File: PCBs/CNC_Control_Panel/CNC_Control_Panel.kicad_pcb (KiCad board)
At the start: 2 copper layers, 65 x 56 mm, 22 parts, among them J1 Conn_01x07_Male, P1 Conn_02x20_Odd_Even, X0 SW_Push, Y0 SW_Push

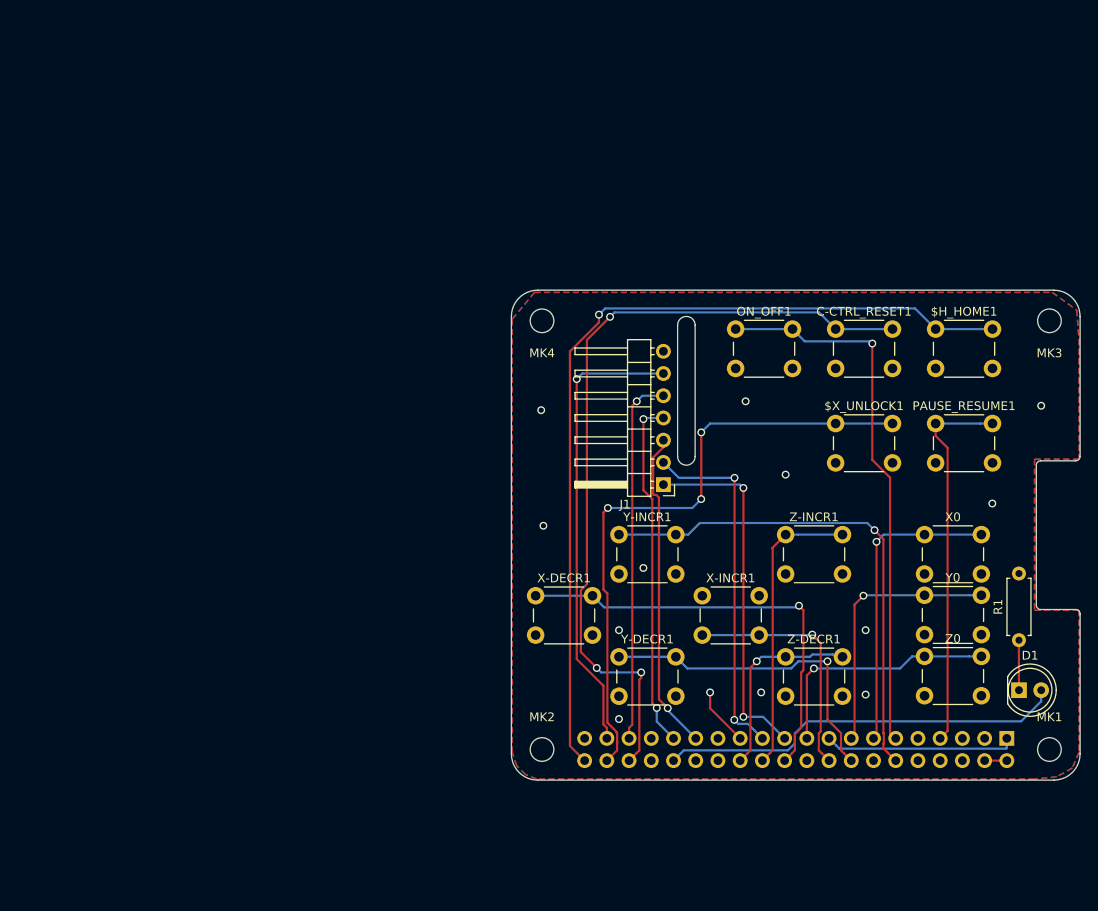
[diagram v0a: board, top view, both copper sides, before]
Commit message: new layout with a 100x100mm board design and cutout for a 8mm rotatary switch
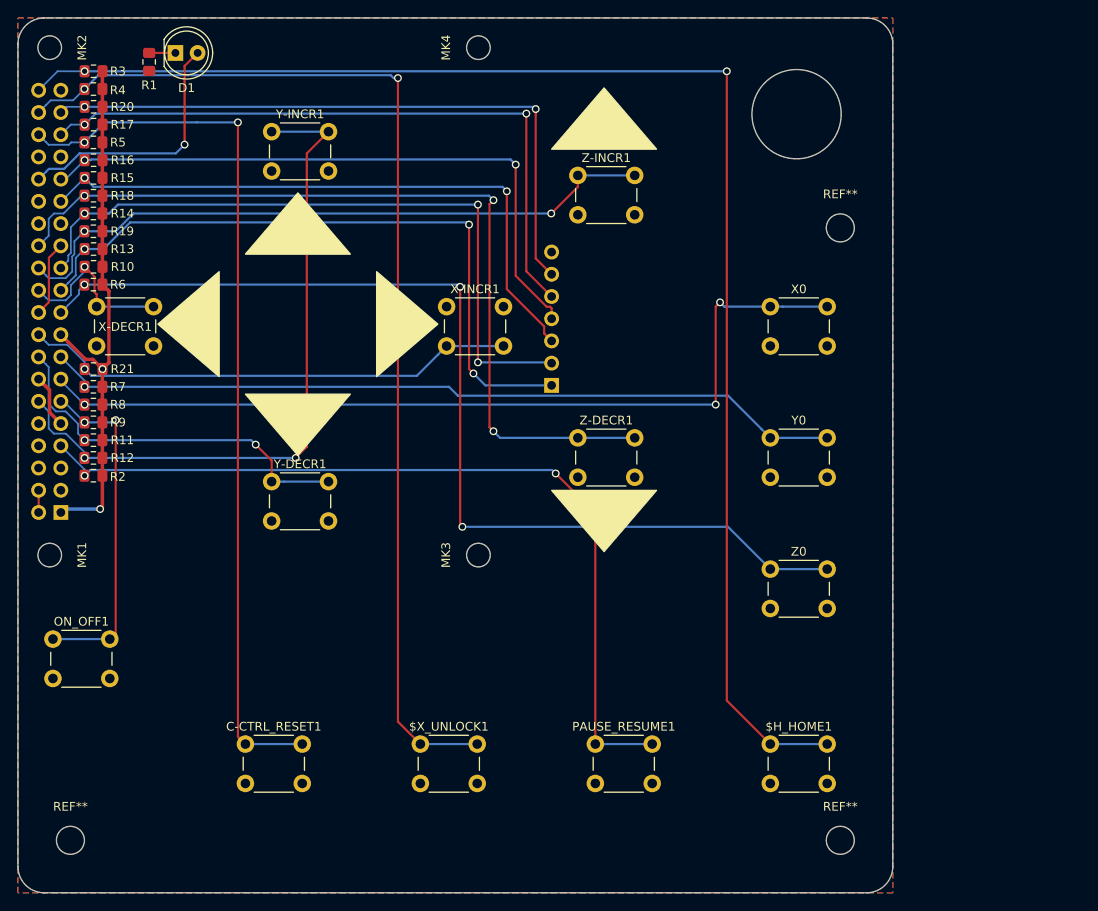
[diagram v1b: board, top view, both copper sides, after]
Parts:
- added R10: 10k, Resistor_SMD:R_0805_2012Metric_Pad1.15x1.40mm_HandSolder, F.Cu at (152.6, 91.4)
- added R11: 10k, Resistor_SMD:R_0805_2012Metric_Pad1.15x1.40mm_HandSolder, F.Cu at (152.6, 111.3)
- added R12: 10k, Resistor_SMD:R_0805_2012Metric_Pad1.15x1.40mm_HandSolder, F.Cu at (152.6, 113.3)
- added R13: 10k, Resistor_SMD:R_0805_2012Metric_Pad1.15x1.40mm_HandSolder, F.Cu at (152.6, 89.4)
- added R14: 10k, Resistor_SMD:R_0805_2012Metric_Pad1.15x1.40mm_HandSolder, F.Cu at (152.6, 85.4)
- added R15: 10k, Resistor_SMD:R_0805_2012Metric_Pad1.15x1.40mm_HandSolder, F.Cu at (152.6, 81.3)
- added R16: 10k, Resistor_SMD:R_0805_2012Metric_Pad1.15x1.40mm_HandSolder, F.Cu at (152.6, 79.3)
- added R17: 10k, Resistor_SMD:R_0805_2012Metric_Pad1.15x1.40mm_HandSolder, F.Cu at (152.6, 75.2)
- added R18: 10k, Resistor_SMD:R_0805_2012Metric_Pad1.15x1.40mm_HandSolder, F.Cu at (152.6, 83.3)
- added R19: 10k, Resistor_SMD:R_0805_2012Metric_Pad1.15x1.40mm_HandSolder, F.Cu at (152.6, 87.4)
- added R2: 10k, Resistor_SMD:R_0805_2012Metric_Pad1.15x1.40mm_HandSolder, F.Cu at (152.6, 115.3)
- added R20: 10k, Resistor_SMD:R_0805_2012Metric_Pad1.15x1.40mm_HandSolder, F.Cu at (152.6, 73.2)
- added R21: 10k, Resistor_SMD:R_0805_2012Metric_Pad1.15x1.40mm_HandSolder, F.Cu at (152.6, 103.1)
- added R3: 10k, Resistor_SMD:R_0805_2012Metric_Pad1.15x1.40mm_HandSolder, F.Cu at (152.6, 69.1)
- added R4: 10k, Resistor_SMD:R_0805_2012Metric_Pad1.15x1.40mm_HandSolder, F.Cu at (152.6, 71.1)
- added R5: 10k, Resistor_SMD:R_0805_2012Metric_Pad1.15x1.40mm_HandSolder, F.Cu at (152.6, 77.2)
- added R6: 10k, Resistor_SMD:R_0805_2012Metric_Pad1.15x1.40mm_HandSolder, F.Cu at (152.6, 93.5)
- added R7: 10k, Resistor_SMD:R_0805_2012Metric_Pad1.15x1.40mm_HandSolder, F.Cu at (152.6, 105.2)
- added R8: 10k, Resistor_SMD:R_0805_2012Metric_Pad1.15x1.40mm_HandSolder, F.Cu at (152.6, 107.2)
- added R9: 10k, Resistor_SMD:R_0805_2012Metric_Pad1.15x1.40mm_HandSolder, F.Cu at (152.6, 109.2)
- added REF**: MountingHole_3.2mm_M3_ISO7380, MountingHole:MountingHole_3.2mm_M3_ISO7380, F.Cu at (150.0, 157.0)
- added REF**: MountingHole_3.2mm_M3_ISO7380, MountingHole:MountingHole_3.2mm_M3_ISO7380, F.Cu at (238.0, 157.0)
- added REF**: MountingHole_3.2mm_M3_ISO7380, MountingHole:MountingHole_3.2mm_M3_ISO7380, F.Cu at (238.0, 87.0)
- J1: moved to B.Cu
- R1: value R -> 470; footprint Resistor_THT:R_Axial_DIN0207_L6.3mm_D2.5mm_P7.62mm_Horizontal -> Resistor_SMD:R_0805_2012Metric_Pad1.15x1.40mm_HandSolder
- moved D1 120.8 mm to (162.0, 67.0)
- moved R1 119.4 mm to (159.0, 68.0), turned to 270 degrees
- moved MK1 116.4 mm to (147.6, 124.4), turned to 270 degrees
- moved P1 111.2 mm to (148.9, 119.5), turned to 0 degrees
- moved MK2 98.0 mm to (147.6, 66.4), turned to 270 degrees
- moved ON_OFF1 85.7 mm to (148.0, 134.0)
- moved C-CTRL_RESET1 82.5 mm to (170.0, 146.0)
- moved MK3 70.6 mm to (196.6, 124.4), turned to 90 degrees
- moved Y-INCR1 60.8 mm to (173.0, 76.0)
- moved X-DECR1 60.1 mm to (153.0, 96.0)
- moved $X_UNLOCK1 60.0 mm to (190.0, 146.0)
- moved PAUSE_RESUME1 53.4 mm to (210.0, 146.0)
- moved $H_HOME1 51.1 mm to (230.0, 146.0)
- moved Z-INCR1 47.4 mm to (208.0, 81.0)
- moved Y-DECR1 44.5 mm to (173.0, 116.0)
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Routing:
- net /GPIO10(SPI0_MOSI): track 28.0 -> 118.6 mm, vias 1 -> 3
- net /GPIO7(SPI1_CE_N): track 22.4 -> 99.0 mm, vias 1 -> 3
- net /GPIO21(SPI1_SCK): track 99.3 -> 165.0 mm, vias 1 -> 2
- net /GPIO27(GEN2): track 34.9 -> 100.5 mm, vias 1 -> 3
- net /GPIO22(GEN3): track 30.4 -> 91.8 mm
- net /GPIO4(GCLK): track 43.4 -> 98.1 mm, vias 0 -> 2
- net /GPIO20(SPI1_MOSI): track 72.3 -> 126.7 mm, vias 3 -> 2
- net /GPIO8(SPI0_CE_N): track 33.5 -> 76.1 mm, vias 0 -> 2
- net +3V3: track 21.9 -> 61.8 mm, vias 0 -> 2
- net /GPIO11(SPI0_SCK): track 40.6 -> 79.2 mm, vias 2 -> 3
- net /GPIO9(SPI0_MISO): track 41.2 -> 77.9 mm, vias 2 -> 3
- net /GPIO5: track 36.8 -> 71.9 mm, vias 1 -> 2
- net /GPIO19(SPI1_MISO): track 42.2 -> 76.3 mm, vias 1 -> 2
- net /GPIO6: track 40.3 -> 72.7 mm
- net /GPIO25(GEN6): track 49.5 -> 19.9 mm
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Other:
- board size 65 x 56 mm -> 100 x 100 mm
- board text removed: "CAMERA"
